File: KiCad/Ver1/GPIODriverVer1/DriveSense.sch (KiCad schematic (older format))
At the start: 6 parts

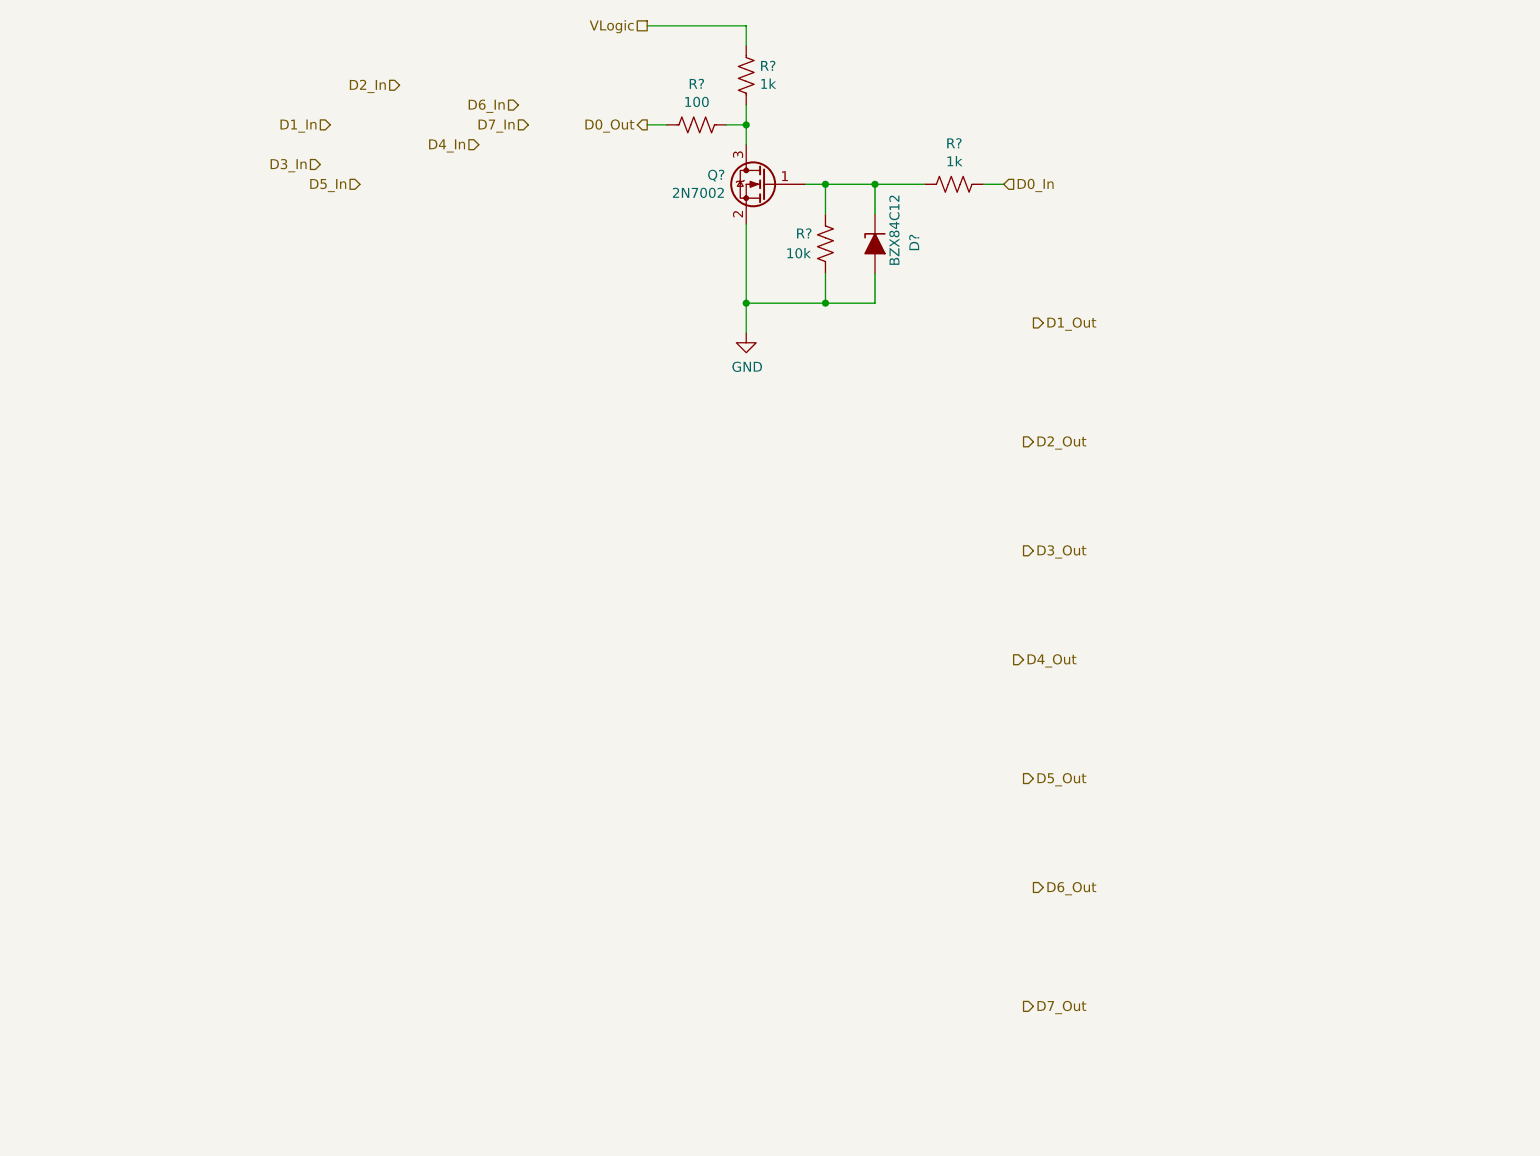
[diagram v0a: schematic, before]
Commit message: Updated schematic to include input/output buffers. Added connections for shift registers.
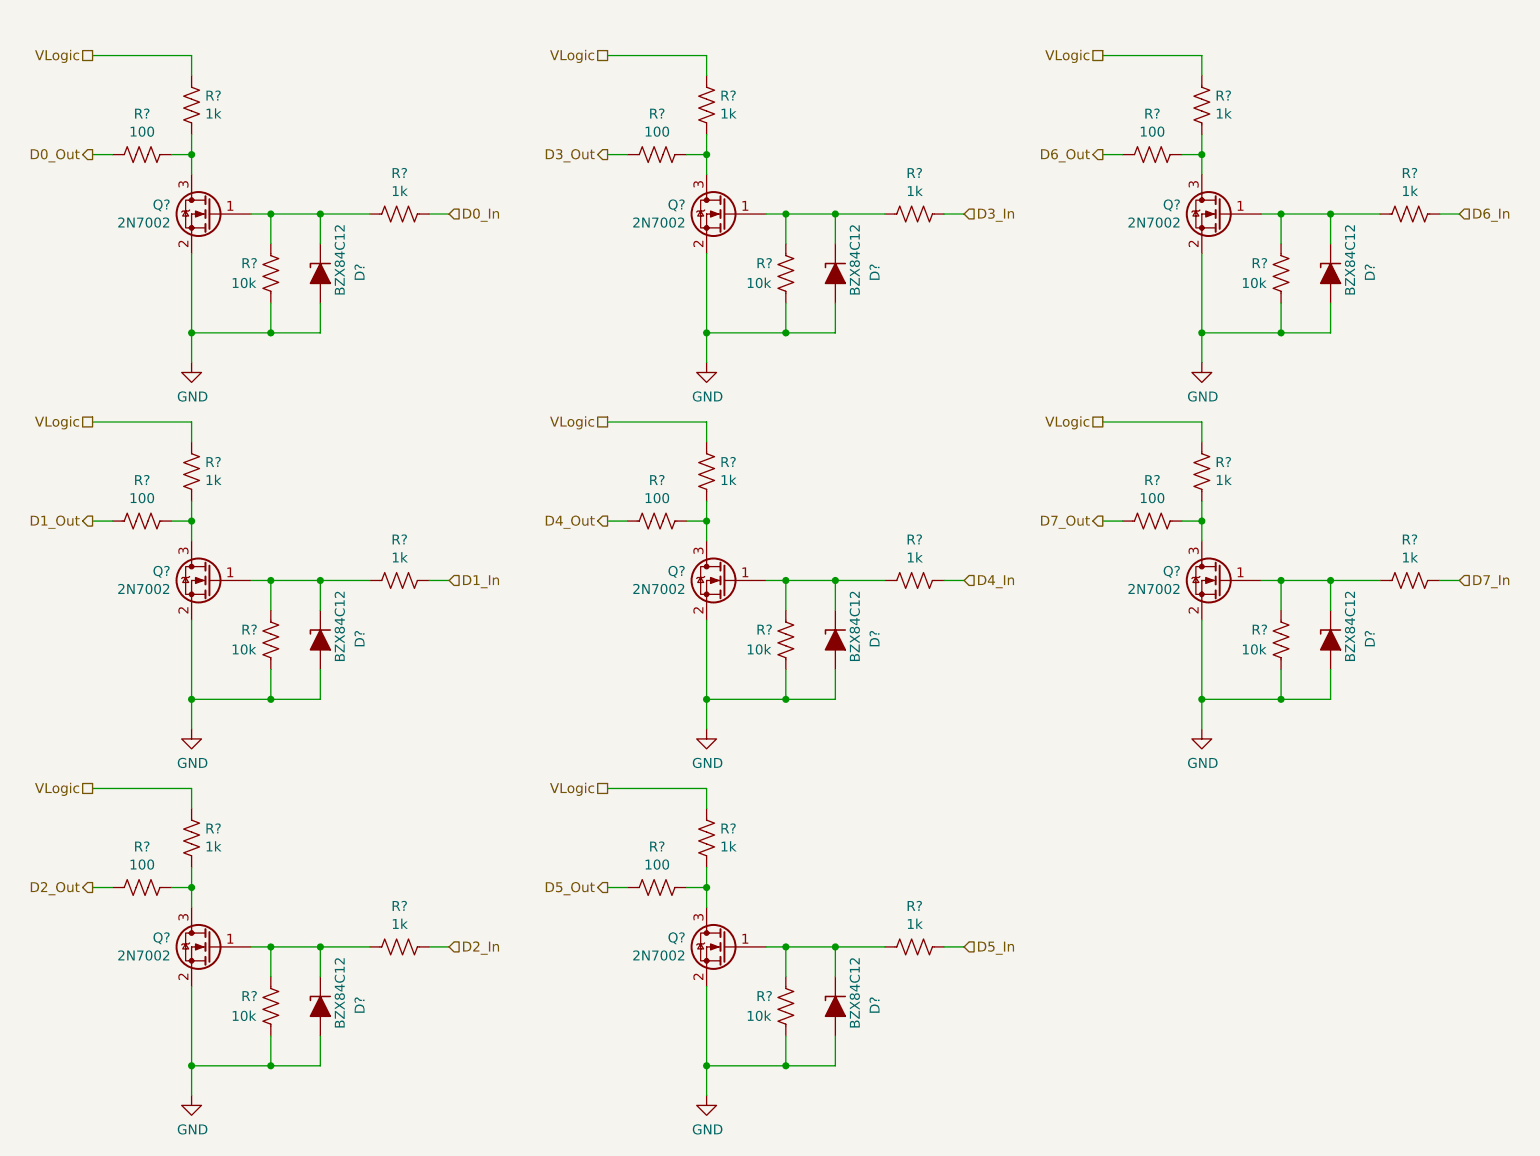
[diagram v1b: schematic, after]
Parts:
- added D? (x7): BZX84C12, symbol Device:D_Zener_ALT
- added Q? (x7): 2N7002, Package_TO_SOT_SMD:SOT-23, symbol Transistor_FET:2N7002
- added R? (x7): 100, symbol Device:R_US
- added R? (x14): 1k, symbol Device:R_US
- added R? (x7): 10k, symbol Device:R_US
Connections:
- net D1_In: now also R?.1
- net D1_Out: now also R?.2
- net D2_In: now also R?.1
- net D2_Out: now also R?.2
- net D3_In: now also R?.1
- net D3_Out: now also R?.2
- net D4_In: now also R?.1
- net D4_Out: now also R?.2
- net D5_In: now also R?.1
- net D5_Out: now also R?.2
- net D6_In: now also R?.1
- net D6_Out: now also R?.2
- net D7_In: now also R?.1
- net D7_Out: now also R?.2
- net GND: now also D?.2 (A), D?.2 (A), D?.2 (A), D?.2 (A), D?.2 (A), D?.2 (A), D?.2 (A), Q?.2 (S), Q?.2 (S), Q?.2 (S), Q?.2 (S), Q?.2 (S), Q?.2 (S), Q?.2 (S), R?.2, R?.2, R?.2, R?.2, R?.2, R?.2, R?.2
- net VLogic: now also R?.1, R?.1, R?.1, R?.1, R?.1, R?.1, R?.1
- new net: Q?.3 (D), R?.1, R?.2 (x7)
- new net: D?.1 (K), Q?.1 (G), R?.1, R?.2 (x7)
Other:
- moved on the sheet: D?, Q?, R?

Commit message: Save point Ver1 design.
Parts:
- D25, D26, D27, D28, D29, D30, D31, D32: renamed from D?; footprint (none) -> Diode_SMD:D_SOT-23_ANK
- R65, R66, R67, R68, R69, R70, R71, R72, R73, R74, R75, R76, R77, R78, R79, R80, R81, R82, R83, R84, R85, R86, R87, R88, R89, R90, R91, R92, R93, R94, R95, R96: renamed from R?; footprint (none) -> Resistor_SMD:R_0402_1005Metric
- gave numbers to parts that had none: 8
